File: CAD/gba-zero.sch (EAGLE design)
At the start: 62 parts, among them IC5 APX803, Q2 BSS138, SW1 LEFT, SW2 RIGHT, SW3 PWR_SWITCH, U1 NC7WZ16, U4 LM4875, X1 LINK_SOCKET, X2 HEADPHONE

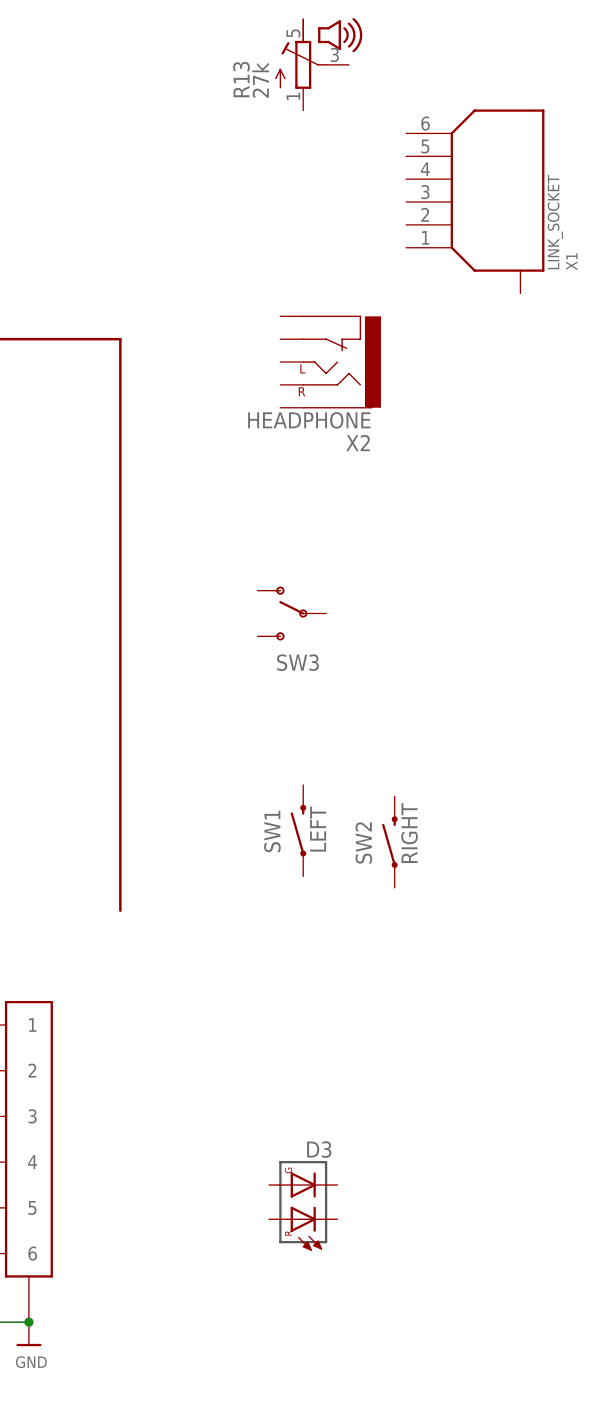
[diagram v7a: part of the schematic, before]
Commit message: Started the layout. Tweaking parts as necessary
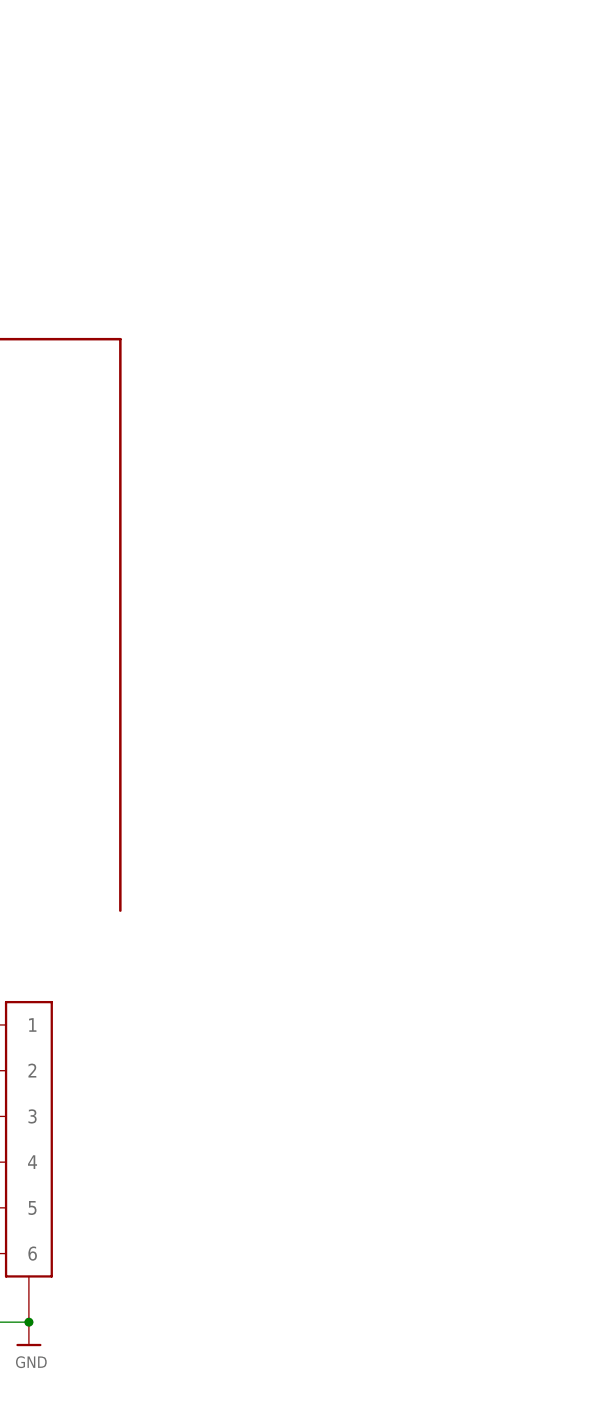
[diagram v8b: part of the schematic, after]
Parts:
- removed D3: DUAL_LED, GBA:DUAL_LED
- removed R13: 27k, GBA:VOLUME
- removed SW1: LEFT, GBA:BUTTON
- removed SW2: RIGHT, GBA:BUTTON
- removed SW3: PWR_SWITCH, GBA:PWR_SWITCH
- removed X1: LINK_SOCKET, GBA:LINK_SOCKET
- removed X2: HEADPHONE, GBA:HEADPHONE
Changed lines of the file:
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@@
 <part name="CN1" library="gba-zero-parts" deviceset="JST_2PIN" device=""/>
 <part name="U$22" library="microbuilder" deviceset="GND" device=""/>
-<part name="X1" library="GBA" deviceset="LINK_SOCKET" device=""/>
-<part name="R13" library="GBA" deviceset="VOLUME" device="" value="27k"/>
-<part name="X2" library="GBA" deviceset="HEADPHONE" device=""/>
-<part name="SW1" library="GBA" deviceset="BUTTON" device="" value="LEFT"/>
-<part name="SW2" library="GBA" deviceset="BUTTON" device="" value="RIGHT"/>
-<part name="SW3" library="GBA" deviceset="PWR_SWITCH" device=""/>
-<part name="D3" library="GBA" deviceset="DUAL_LED" device=""/>
 </parts>
 <sheets>
@@
 <instance part="CN1" gate="G$1" x="180.34" y="177.8" rot="R180"/>
 <instance part="U$22" gate="G$1" x="187.96" y="170.18"/>
-<instance part="X1" gate="X$1" x="285.75" y="261.62" rot="MR90"/>
-<instance part="R13" gate="R$1" x="269.24" y="279.4"/>
-<instance part="X2" gate="X$1" x="276.86" y="243.84" rot="R180"/>
-<instance part="SW1" gate="SW$1" x="269.24" y="194.31" rot="R90"/>
-<instance part="SW2" gate="SW$1" x="279.4" y="193.04" rot="R90"/>
-<instance part="SW3" gate="SW$2" x="266.7" y="218.44" smashed="yes" rot="MR0">
-<attribute name="NAME" x="271.145" y="212.09" size="1.778" layer="95" rot="MR0"/>
-</instance>
-<instance part="D3" gate="D$1" x="270.51" y="154.94" rot="R90"/>
 </instances>
 <busses>
